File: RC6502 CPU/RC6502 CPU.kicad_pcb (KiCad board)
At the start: 2 copper layers, 99.1 x 49.5 mm, 10 parts, among them J1 CONN_01X39, J2 IRQ OnBus, J3 NMI OnBus, U1 WD65C02, U2 74HCT04

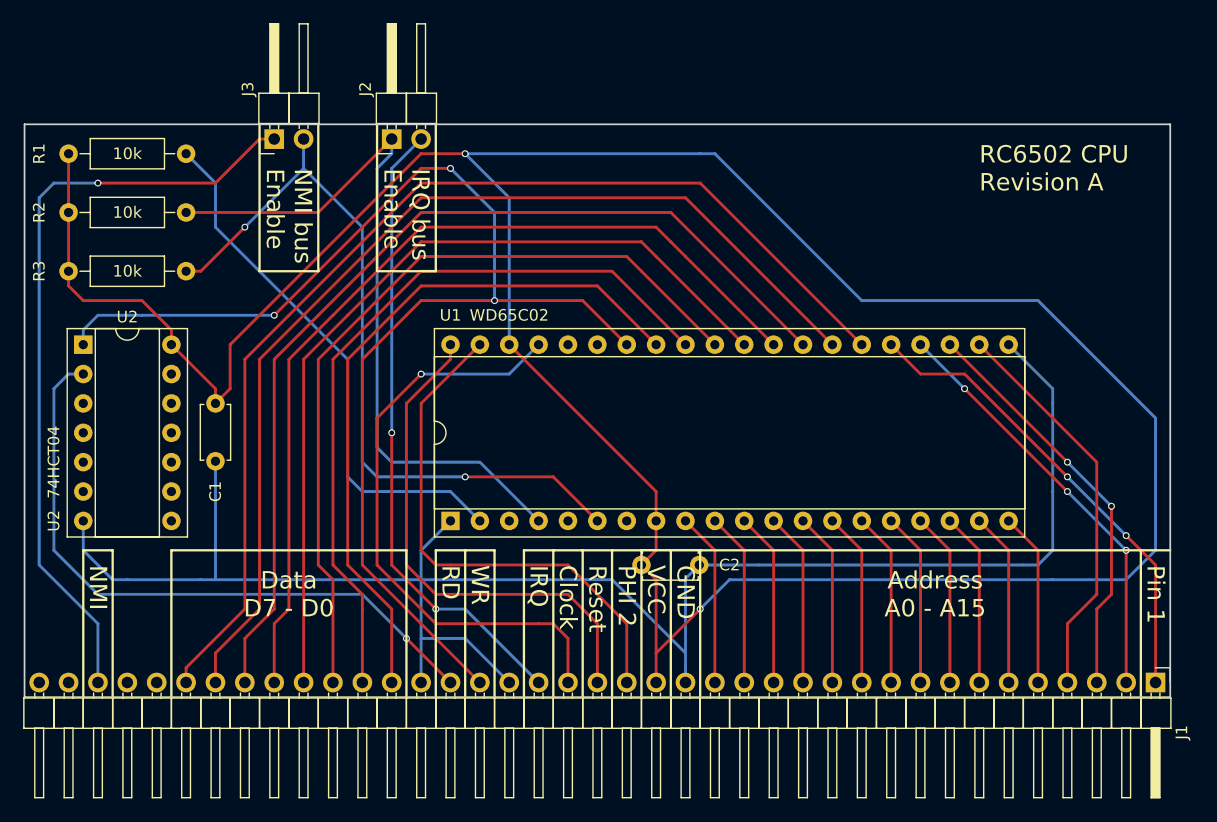
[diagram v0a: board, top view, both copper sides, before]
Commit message: Added oscillator to CPU board
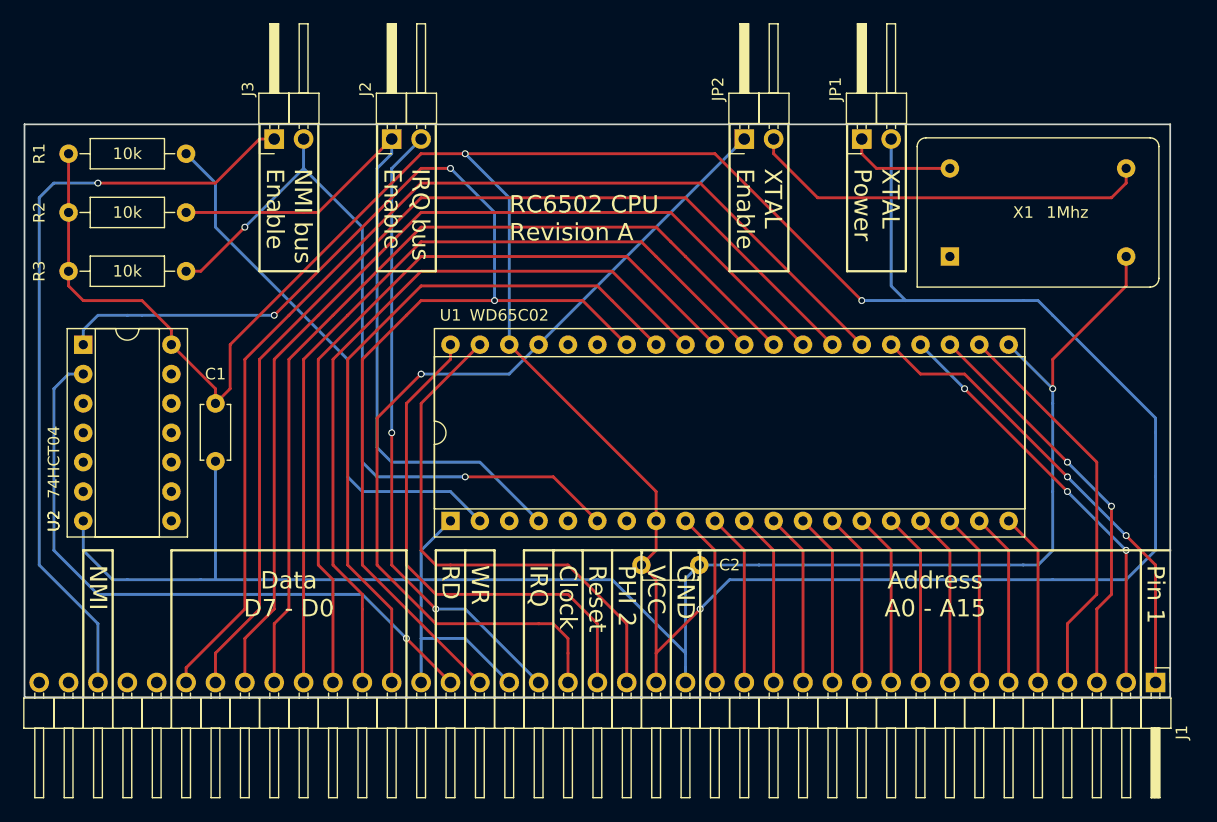
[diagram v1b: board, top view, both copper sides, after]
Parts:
- added JP1: XTAL Power, Pin_Headers:Pin_Header_Angled_1x02_Pitch2.54mm, F.Cu at (165.1, 92.7)
- added JP2: XTAL Enable, Pin_Headers:Pin_Header_Angled_1x02_Pitch2.54mm, F.Cu at (154.9, 92.7)
- added X1: 1Mhz, Oscillators:Oscillator_DIP-14, F.Cu at (172.7, 102.9)
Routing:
- net Net-(JP2-Pad2): track 0.00 -> 35.1 mm
- net CLOCK: track 52.3 -> 77.4 mm
- net VCC: track 243.7 -> 258.1 mm, vias 2 -> 3
- net GND: track 155.1 -> 169.2 mm, vias 0 -> 1
- net Net-(JP1-Pad1): track 0.00 -> 9.42 mm
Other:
- board text added: "XTAL Enable"
- board text added: "XTAL Power"

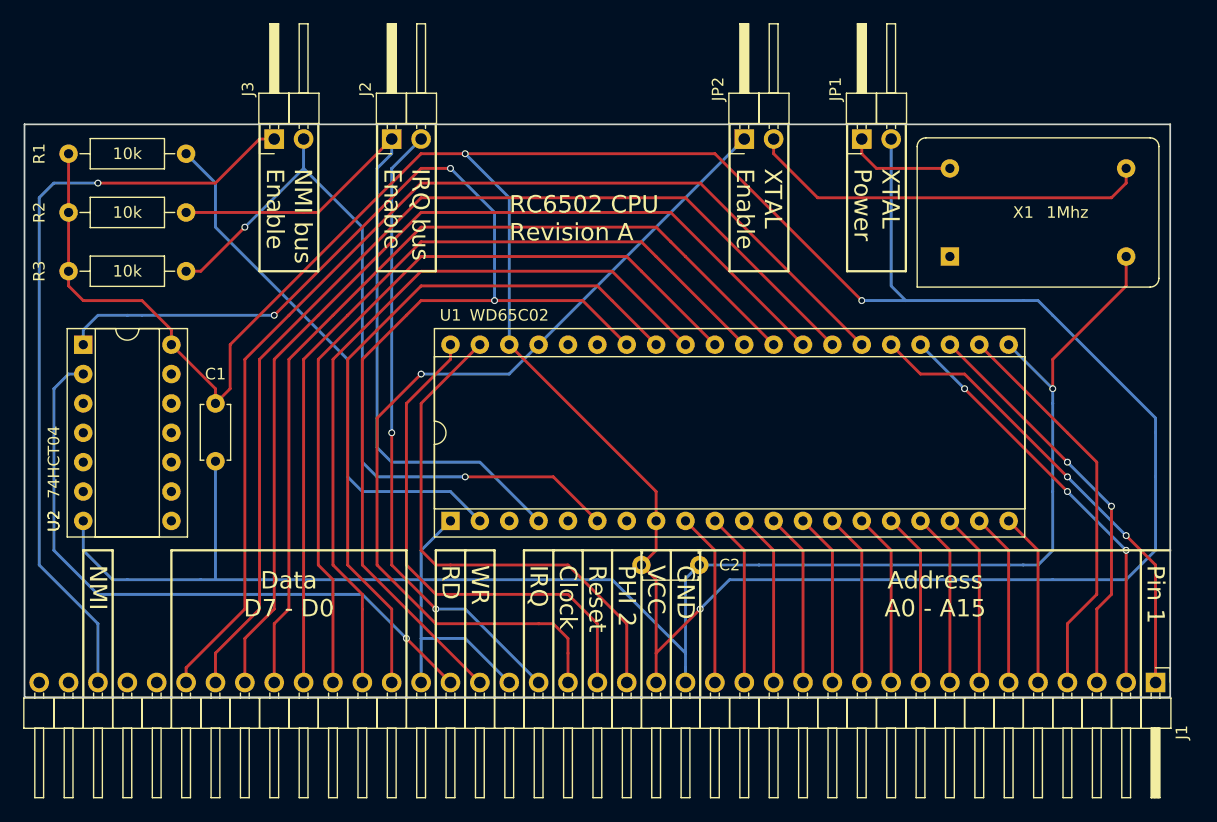
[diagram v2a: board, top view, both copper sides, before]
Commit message: CPU revision B
VP pin was added for W65c02, added SYNC and RDY pins and removed hex inverter.
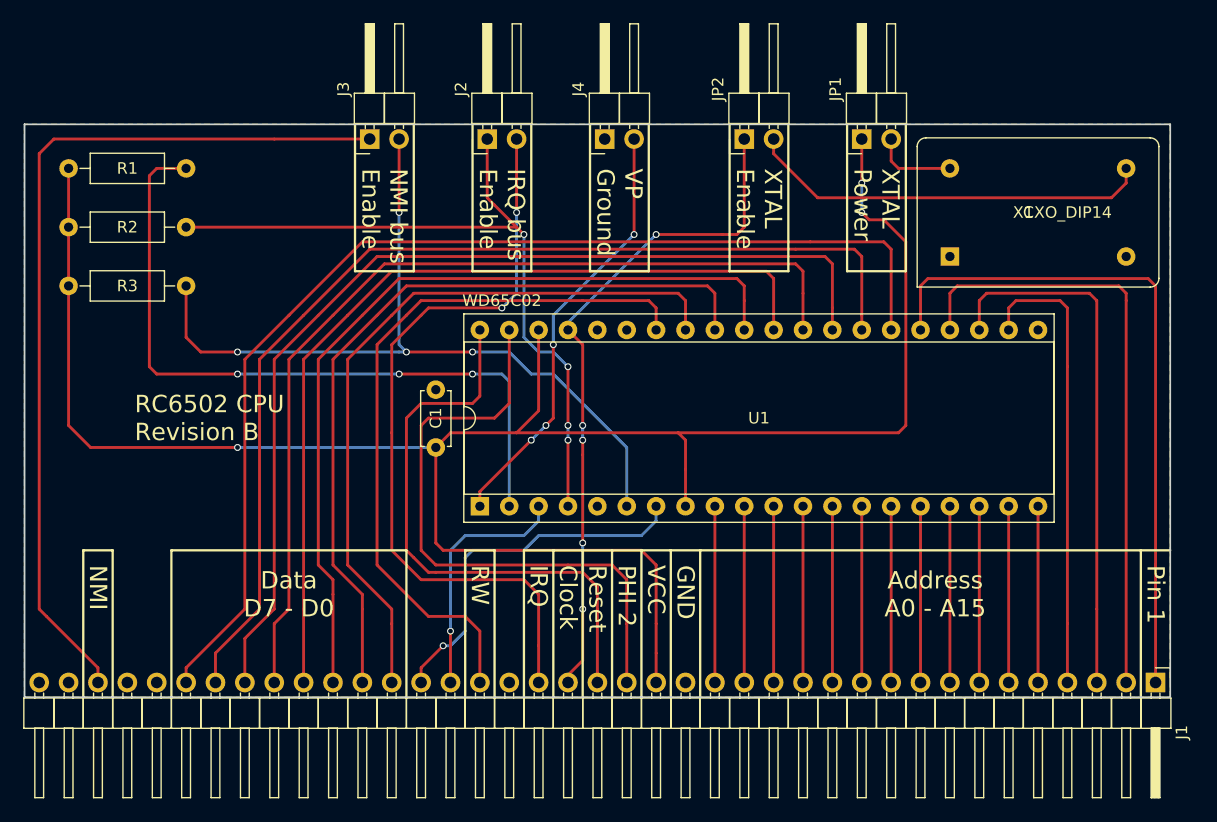
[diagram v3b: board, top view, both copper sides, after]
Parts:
- removed C2: 100nF, Capacitors_THT:C_Disc_D4.7mm_W2.5mm_P5.00mm
- removed U2: 74HCT04, Housings_DIP:DIP-14_W7.62mm_Socket
- added J4: VP GND, Pin_Headers:Pin_Header_Angled_1x02_Pitch2.54mm, F.Cu at (142.9, 92.7)
- R1, R2, R3: value 10k -> 3.3k
- X1: value 1Mhz -> CXO_DIP14
- moved C1 19.4 mm to (128.3, 119.4), turned to 90 degrees
- moved J2 8.26 mm to (132.7, 92.7)
- moved J3 8.26 mm to (122.6, 92.7)
- moved U1 2.84 mm to (132.1, 124.5)
- moved R1 1.27 mm to (106.7, 95.2)
- moved R2 1.27 mm to (106.7, 100.3)
- moved R3 1.27 mm to (106.7, 105.4)
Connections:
- net R/W renamed RW
- J1 pad 23: GND -> (no net)
- J1 pad 25: RD -> RDY
- J1 pad 26: GND -> SYNC
- JP1 pad 1: Net-(JP1-Pad1) -> VCC
- JP1 pad 2: VCC -> Net-(JP1-Pad2)
- U1 pad 1: GND -> Net-(J4-Pad2)
- U1 pad 3: (no net) -> RDY
- U1 pad 7: (no net) -> SYNC
- X1 pad 14: Net-(JP1-Pad1) -> Net-(JP1-Pad2)
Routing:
- net GND: track 169.2 -> 0.00 mm, vias 1 -> 0
- net VCC: track 258.1 -> 177.8 mm
- net RD: track 56.1 -> 0.00 mm, vias 1 -> 0
- net RW: track 110.5 -> 62.6 mm, vias 3 -> 0
- net Net-(J4-Pad2): track 0.00 -> 37.3 mm, vias 0 -> 4
- net SYNC: track 0.00 -> 31.8 mm, vias 0 -> 1
- net RDY: track 0.00 -> 21.4 mm, vias 0 -> 1
- net CLOCK: track 77.4 -> 58.4 mm, vias 1 -> 5
- net A15: track 40.9 -> 58.9 mm, vias 2 -> 0
- net A14: track 36.6 -> 52.6 mm, vias 3 -> 0
- net Net-(R1-Pad1): track 46.7 -> 62.4 mm, vias 0 -> 3
- net IRQ: track 54.8 -> 65.6 mm
- net A13: track 35.5 -> 46.2 mm, vias 2 -> 0
- net NMI: track 66.4 -> 76.9 mm, vias 1 -> 0
- net Net-(JP1-Pad1): track 9.42 -> 0.00 mm
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- added copper zone on B.Cu, net GND
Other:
- board text added: "RC6502 CPU Revision B"
- board text added: "RW"
- board text added: "VP Ground"
- board text removed: "RC6502 CPU Revision A"
- board text removed: "RD"
- board text removed: "WR"

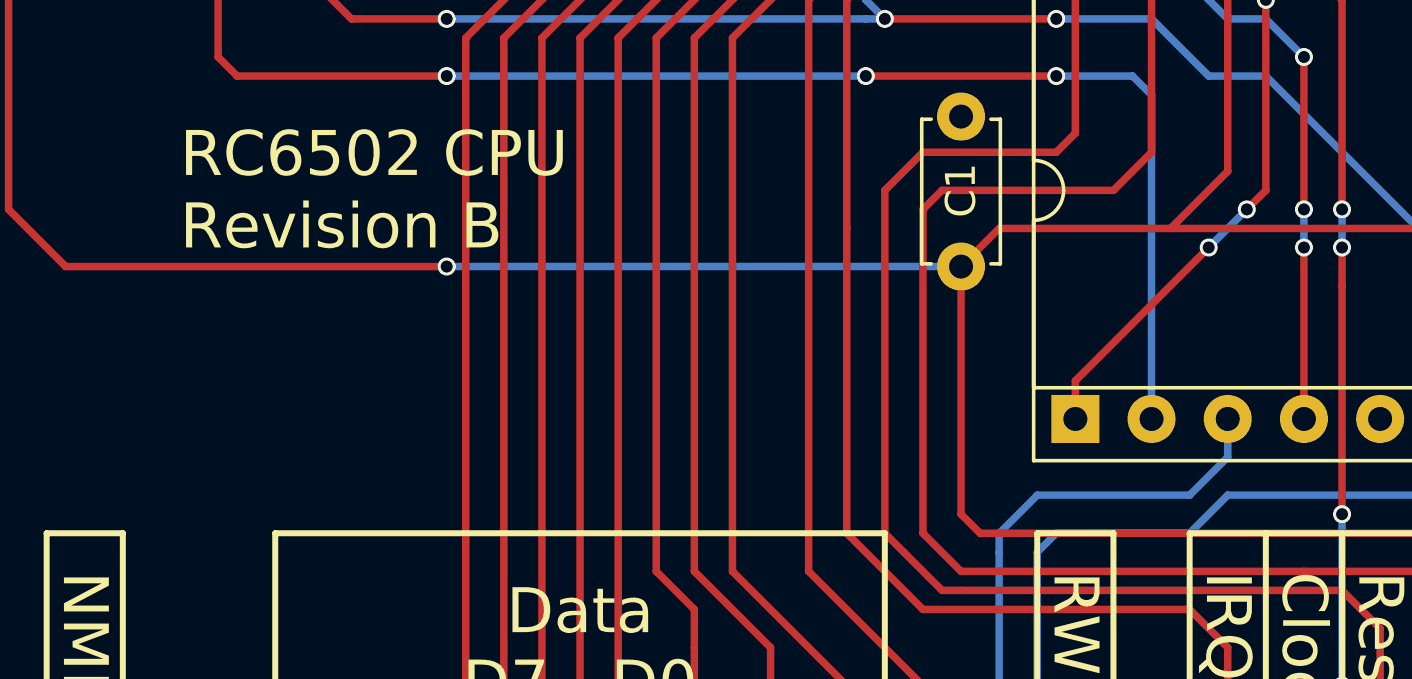
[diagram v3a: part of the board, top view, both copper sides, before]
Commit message: Connected RDY to the wrong pin. Ooops!
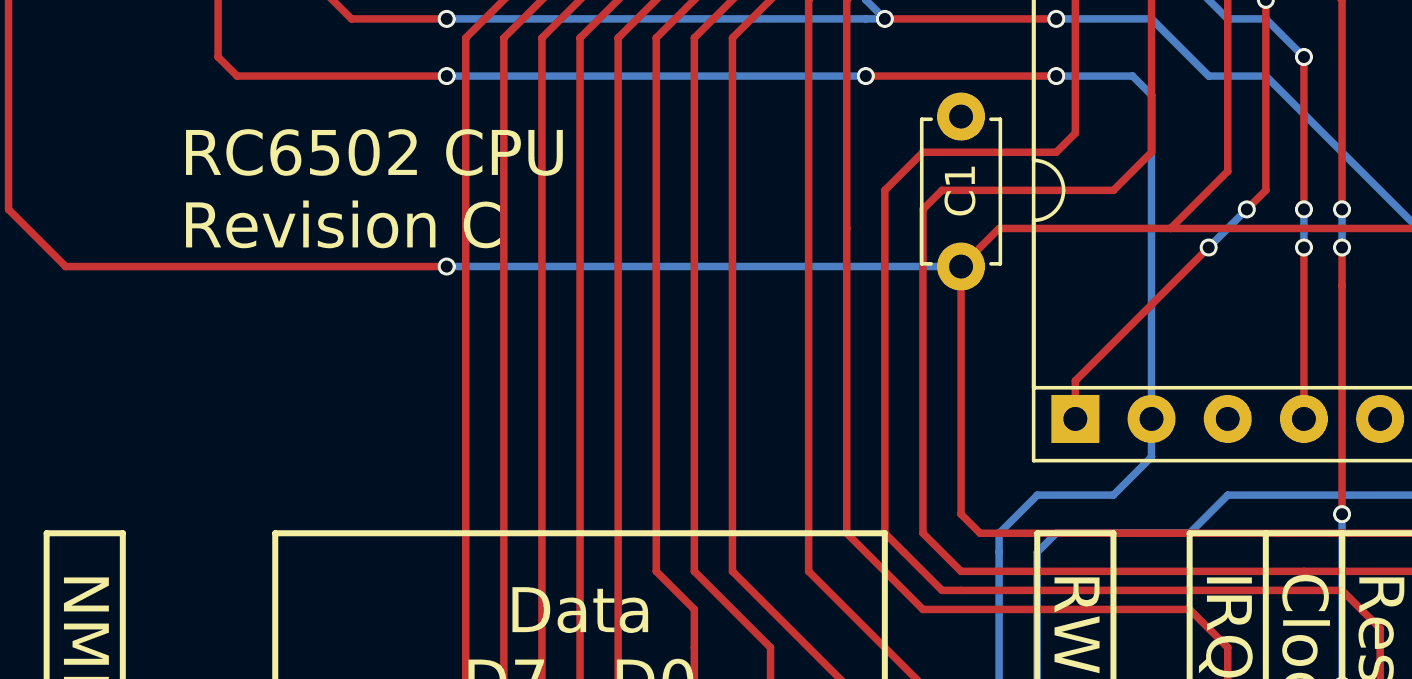
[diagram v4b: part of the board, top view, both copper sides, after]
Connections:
- R1 pad 1: Net-(R1-Pad1) -> RDY
- U1 pad 2: Net-(R1-Pad1) -> RDY
- U1 pad 3: RDY -> (no net)
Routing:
- net Net-(R1-Pad1): track 62.4 -> 0.00 mm, vias 3 -> 0
- net RDY: track 21.4 -> 81.2 mm, vias 1 -> 4
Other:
- board text added: "RC6502 CPU Revision C"
- board text removed: "RC6502 CPU Revision B"
